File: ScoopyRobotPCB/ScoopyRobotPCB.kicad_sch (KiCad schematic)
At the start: 40 parts, among them J1 18V battery, J2 Raspberry_Pi_Header, J3 Left colour sensor, J4 Right colour sensor, J5 Wheels, J6 Power, J7 Left, J8 Right, M1 Chain gearmotor, M2 Left motor, M3 Right motor, Q1 Q_NPN_Darlington_BCE, SW1 SW_Push, SW2 Emergency stop, SW3 Roller position

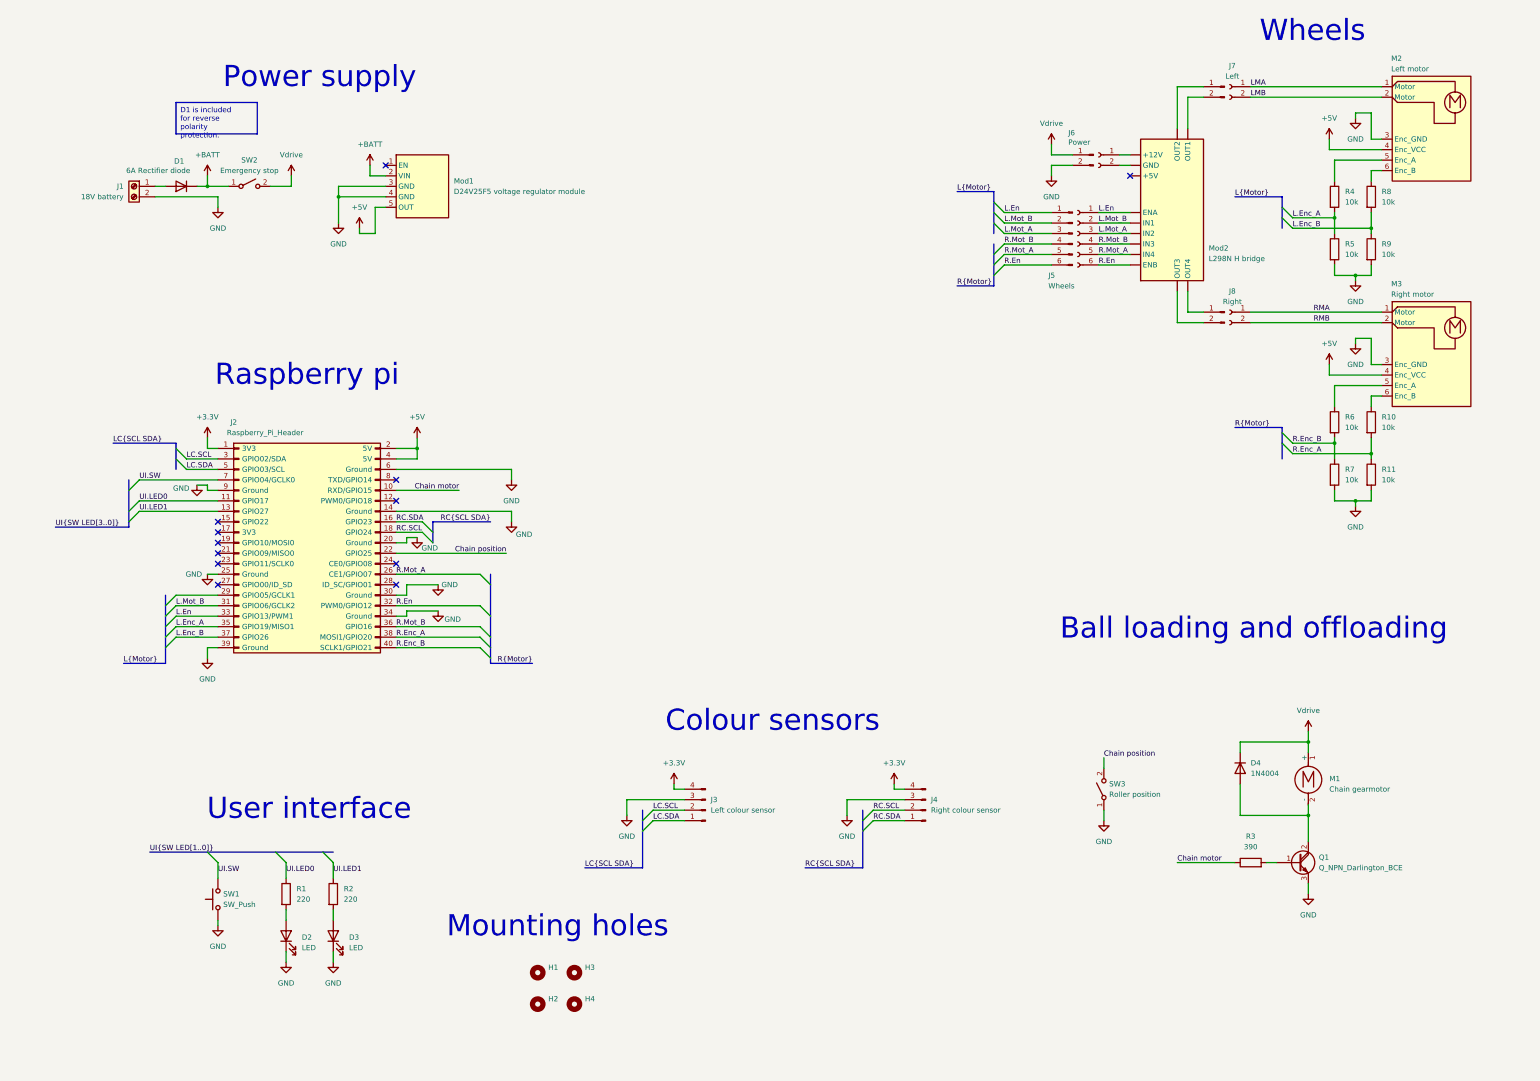
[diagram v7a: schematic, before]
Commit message: Updated the PCB files to match reality
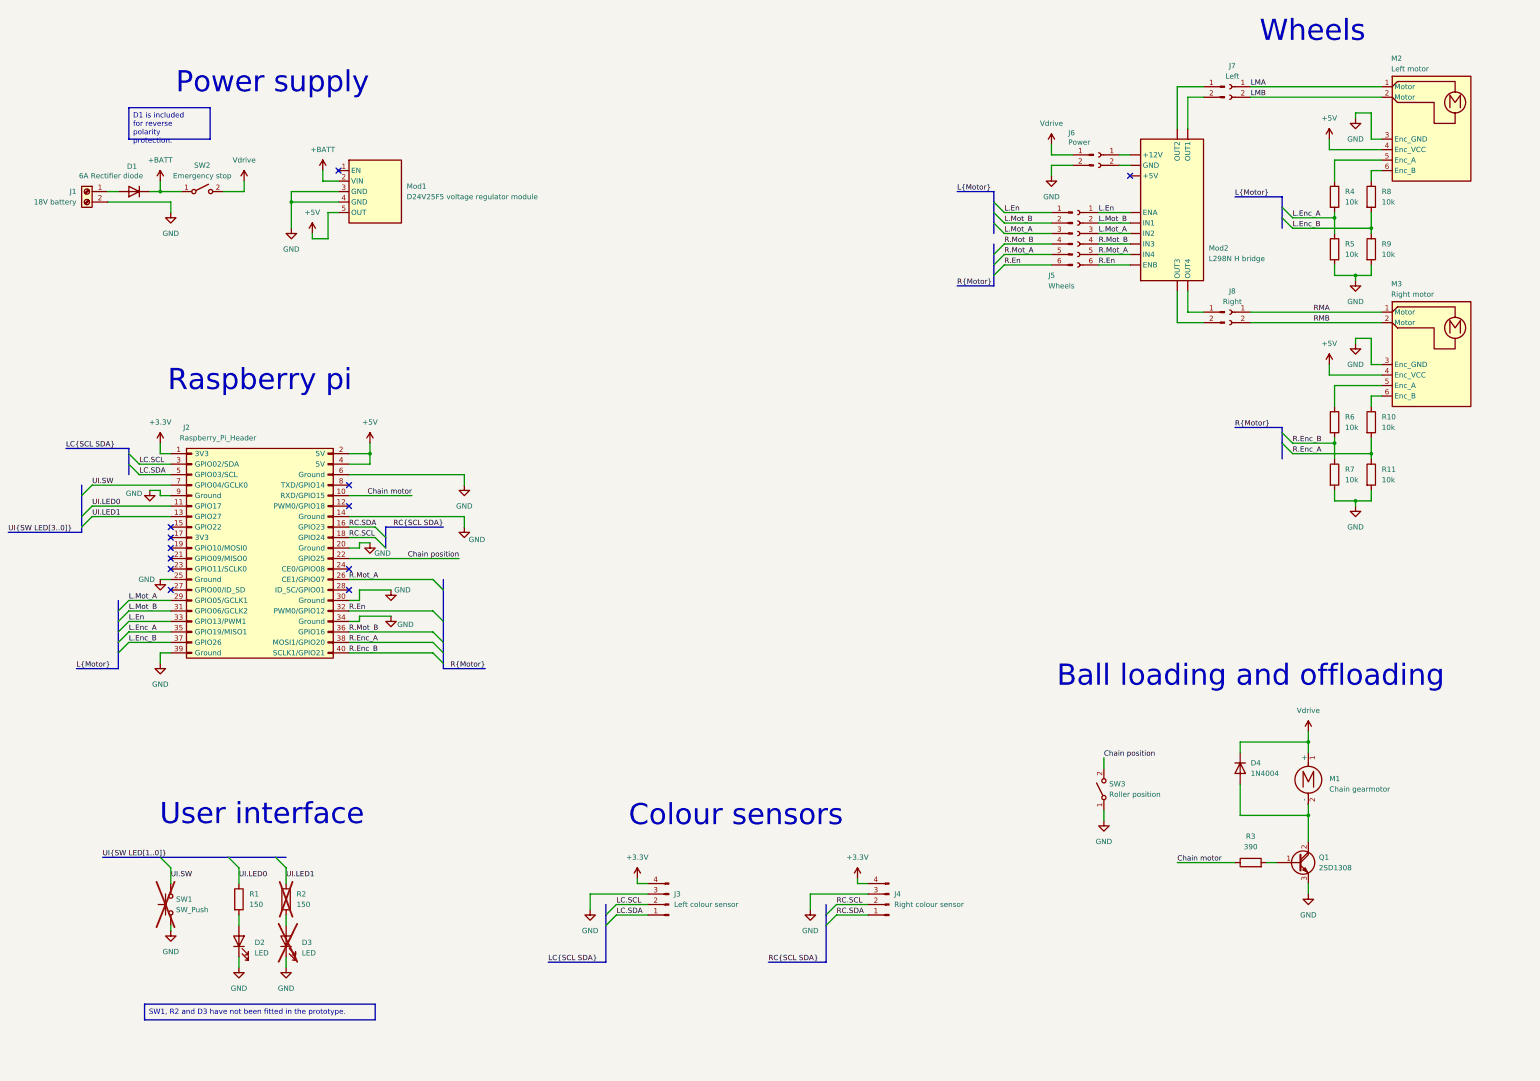
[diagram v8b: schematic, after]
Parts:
- removed H1, H2, H3, H4: MountingHole, MountingHole:MountingHole_3.2mm_M3, symbol Mechanical:MountingHole
- D1: footprint Diode_THT:D_DO-201_P15.24mm_Horizontal -> Diode_THT:D_5KP_P10.16mm_Horizontal
- D3, SW1: now not fitted; now left out of the parts list
- J6: footprint Connector_PinHeader_2.54mm:PinHeader_1x02_P2.54mm_Vertical -> TerminalBlock_Phoenix:TerminalBlock_Phoenix_MKDS-1,5-2_1x02_P5.00mm_Horizontal
- Mod1: footprint Connector_PinHeader_2.54mm:PinHeader_1x05_P2.54mm_Vertical -> Connector_PinSocket_2.54mm:PinSocket_1x05_P2.54mm_Vertical
- Q1: value Q_NPN_Darlington_BCE -> 2SD1308
- R1: value 220 -> 150; footprint Resistor_THT:R_Axial_DIN0411_L9.9mm_D3.6mm_P12.70mm_Horizontal -> Resistor_THT:R_Axial_DIN0207_L6.3mm_D2.5mm_P7.62mm_Horizontal
- R10, R6: footprint Resistor_THT:R_Axial_DIN0411_L9.9mm_D3.6mm_P7.62mm_Vertical -> Resistor_THT:R_Axial_DIN0207_L6.3mm_D2.5mm_P7.62mm_Horizontal
- R11, R3: footprint Resistor_THT:R_Axial_DIN0411_L9.9mm_D3.6mm_P5.08mm_Vertical -> Resistor_THT:R_Axial_DIN0207_L6.3mm_D2.5mm_P5.08mm_Vertical
- R2: value 220 -> 150; now not fitted; now left out of the parts list
- R4, R8: footprint Resistor_THT:R_Axial_DIN0411_L9.9mm_D3.6mm_P7.62mm_Vertical -> Resistor_THT:R_Axial_DIN0207_L6.3mm_D2.5mm_P2.54mm_Vertical
- R5: footprint Resistor_THT:R_Axial_DIN0207_L6.3mm_D2.5mm_P2.54mm_Vertical -> Resistor_THT:R_Axial_DIN0207_L6.3mm_D2.5mm_P5.08mm_Vertical
- R7: footprint Resistor_THT:R_Axial_DIN0309_L9.0mm_D3.2mm_P2.54mm_Vertical -> Resistor_THT:R_Axial_DIN0207_L6.3mm_D2.5mm_P2.54mm_Vertical
- R9: footprint Resistor_THT:R_Axial_DIN0411_L9.9mm_D3.6mm_P5.08mm_Vertical -> Resistor_THT:R_Axial_DIN0207_L6.3mm_D2.5mm_P2.54mm_Vertical
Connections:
- net L.Mot_A: now also J2.29 (GPIO05/GCLK1)
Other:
- note removed: "Mounting holes"
- moved on the sheet: D1, D2, J1, J2, J3, J4, Mod1, R1, SW2
